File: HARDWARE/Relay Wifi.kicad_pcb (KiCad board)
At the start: 2 copper layers, 43 parts, among them J1 Bornera 01x02, J10 Screw_Terminal_01x03, J11 HC-SR04, J2 Screw_Terminal_01x03, J3 Screw_Terminal_01x03, J4 Screw_Terminal_01x03, J5 Screw_Terminal_01x03, J6 Screw_Terminal_01x03, J7 Screw_Terminal_01x03, J8 Screw_Terminal_01x03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

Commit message: Agrego carpeta hardware con archivos
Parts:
- removed G***: LOGO, LOGO:Logo relé
- removed J10, J5, J6, J7, J8: Screw_Terminal_01x03, TerminalBlock:TerminalBlock_bornier-3_P5.08mm
- removed SW1: SW_SPDT, EESTN5:Pin_Header_3
- added J12: Screw_Terminal_01x04, TerminalBlock_Altech:Altech_AK100_1x04_P5.00mm, F.Cu at (142.0, 39.8)
- added Switch1: SW_SPDT, EESTN5:Pin_Header_3, F.Cu at (157.8, 88.3)
- J1, J11, J9: moved to B.Cu
- J2, J3, J4: value Screw_Terminal_01x03 -> Screw_Terminal_01x04; footprint TerminalBlock:TerminalBlock_bornier-3_P5.08mm -> TerminalBlock_Altech:Altech_AK100_1x04_P5.00mm
- Q1, Q2, Q3, Q4: footprint EESTN5:to92 -> EESTN5:SOT23
- U2, U3, U5, U6: footprint Package_DIP:DIP-4_W7.62mm -> EESTN5:DIP-4_PC817
- U4: footprint Package_TO_SOT_THT:TO-220-3_Vertical -> Package_TO_SOT_SMD:TO-263-3_TabPin2
- moved J4 88.1 mm to (94.9, 39.8), turned to 180 degrees
- moved R4 83.8 mm to (84.0, 125.9)
- moved J3 82.3 mm to (118.4, 39.8), turned to 180 degrees
- moved J11 74.2 mm to (82.7, 129.8)
- moved U3 65.7 mm to (150.4, 70.9), turned to 0 degrees
- moved R1 58.0 mm to (86.5, 125.9), turned to 90 degrees
- moved R3 55.9 mm to (158.0, 77.8)
- moved U2 54.3 mm to (126.7, 70.9), turned to 0 degrees
- moved D2 50.6 mm to (163.0, 70.9), turned to 0 degrees
- moved J9 49.4 mm to (95.6, 129.8), turned to 0 degrees
- moved Q1 46.0 mm to (162.9, 78.8), turned to 90 degrees
- moved R7 44.9 mm to (134.3, 77.8)
- moved R2 44.3 mm to (110.0, 122.5), turned to -90 degrees
- moved R8 43.6 mm to (112.5, 122.5), turned to -90 degrees
- moved U5 42.9 mm to (103.2, 70.9), turned to 0 degrees
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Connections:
- J2 pad 1: com2 -> com3
- J3 pad 1: Net-(J3-Pin_1) -> com5
- J3 pad 3: com3 -> Net-(J3-Pin_3)
- J4 pad 1: com4 -> com7
- K1 pad 11: Net-(J4-Pin_2) -> unconnected-(K1-Pad11)
- K1 pad 6: Net-(J3-Pin_2) -> unconnected-(K1-Pad6)
- K1 pad 8: Net-(J3-Pin_1) -> Net-(J2-Pin_2)
- K1 pad 9: Net-(J4-Pin_3) -> Net-(J2-Pin_3)
- K2 pad 11: Net-(J8-Pin_2) -> unconnected-(K2-Pad11)
- K2 pad 6: Net-(J6-Pin_2) -> unconnected-(K2-Pad6)
- K2 pad 8: Net-(J6-Pin_1) -> Net-(J3-Pin_2)
- K2 pad 9: Net-(J8-Pin_3) -> Net-(J3-Pin_3)
- K3 pad 11: Net-(J2-Pin_2) -> unconnected-(K3-Pad11)
- K3 pad 6: Net-(J10-Pin_2) -> unconnected-(K3-Pad6)
- K3 pad 9: Net-(J2-Pin_3) -> Net-(J12-Pin_3)
- K4 pad 11: Net-(J7-Pin_2) -> unconnected-(K4-Pad11)
- K4 pad 6: Net-(J5-Pin_2) -> unconnected-(K4-Pad6)
- K4 pad 8: Net-(J5-Pin_1) -> Net-(J4-Pin_2)
- K4 pad 9: Net-(J7-Pin_3) -> Net-(J4-Pin_3)
- U1 pad 27: unconnected-(U1-IO16-Pad27) -> relay_4
- U1 pad 28: unconnected-(U1-IO17-Pad28) -> relay_3
- U1 pad 30: unconnected-(U1-IO18-Pad30) -> relay_2
- U1 pad 31: unconnected-(U1-IO19-Pad31) -> relay_1
- U1 pad 4: ECHO -> unconnected-(U1-SVN-Pad4)
- U1 pad 5: relay_2 -> unconnected-(U1-IO34-Pad5)
- U1 pad 6: relay_1 -> unconnected-(U1-IO35-Pad6)
- U1 pad 7: relay_3 -> ECHO
- U1 pad 8: relay_4 -> TRIGGER
- U1 pad 9: TRIGGER -> unconnected-(U1-IO25-Pad9)
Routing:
- net VCC: track 344.5 -> 175.0 mm, vias 5 -> 0
- net GND: track 0.00 -> 144.2 mm, vias 0 -> 6
- net Net-(R10-Pad2): track 9.08 -> 122.9 mm
- net Net-(R6-Pad2): track 38.8 -> 103.7 mm
- net D1: track 47.2 -> 95.0 mm, vias 2 -> 0
- net Net-(R8-Pad2): track 70.8 -> 103.6 mm
- net Net-(J11-Pin_2): track 31.3 -> 2.90 mm, vias 1 -> 0
- net +5V: track 137.6 -> 163.6 mm, vias 1 -> 0
- net ECHO: track 48.1 -> 71.5 mm, vias 1 -> 0
- net Net-(J7-Pin_2): track 16.0 -> 0.00 mm
- net Net-(J5-Pin_2): track 16.0 -> 0.00 mm
- net Net-(J6-Pin_2): track 15.9 -> 0.00 mm
- net Net-(J10-Pin_2): track 15.9 -> 0.00 mm
- net Net-(J8-Pin_2): track 15.9 -> 0.00 mm
- net Net-(D8-A): track 24.5 -> 38.7 mm
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- removed copper zone on B.Cu, net GND

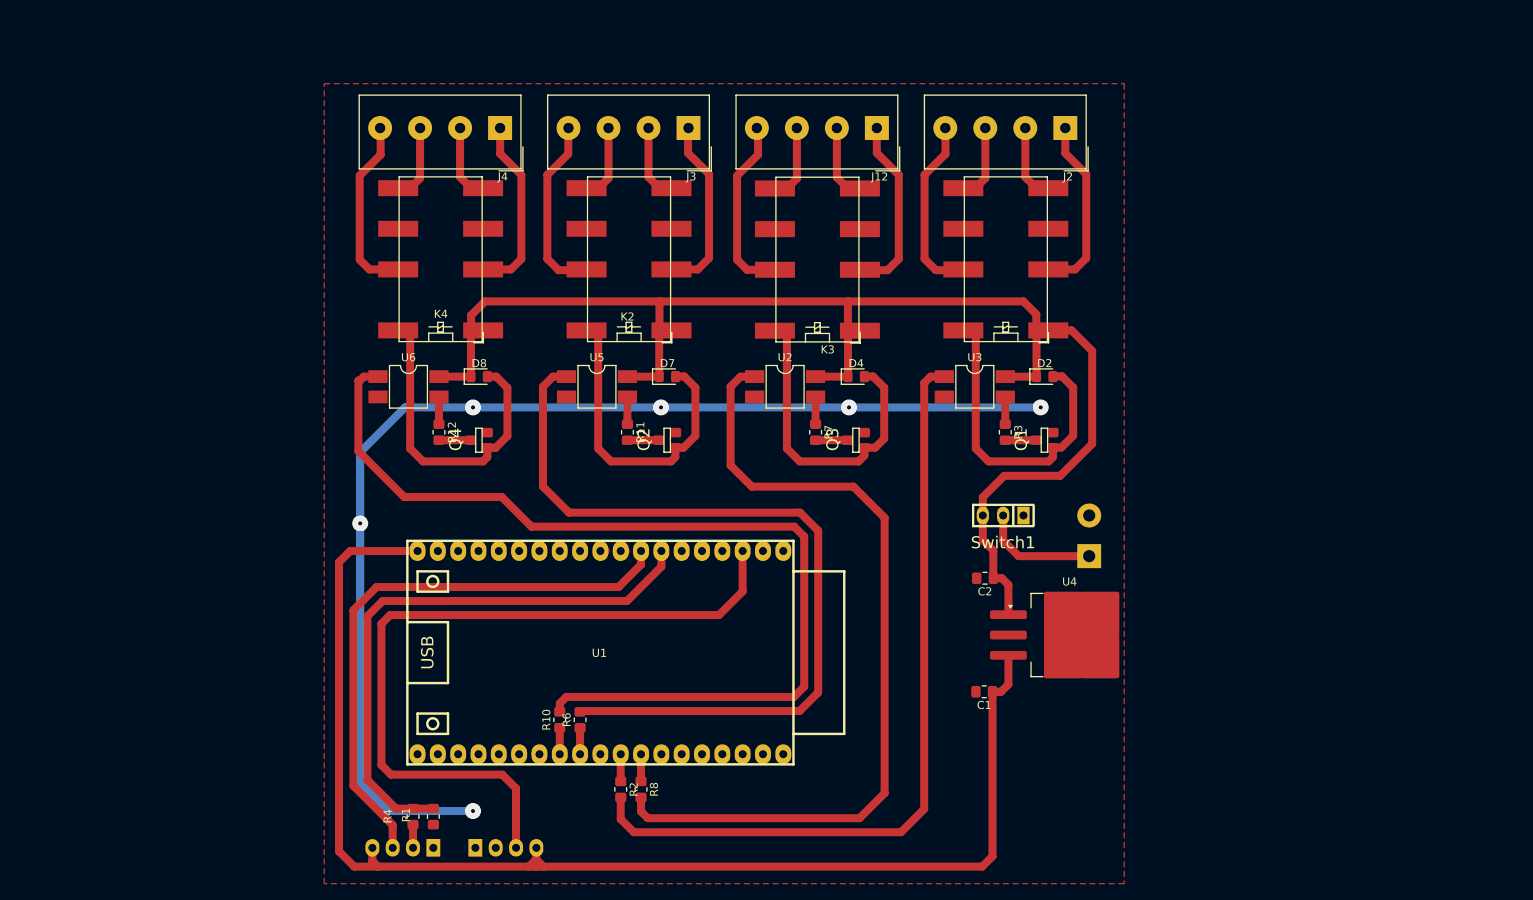
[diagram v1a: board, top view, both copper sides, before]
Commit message: Agrego el nuevo diseño de la placa y el esquematico
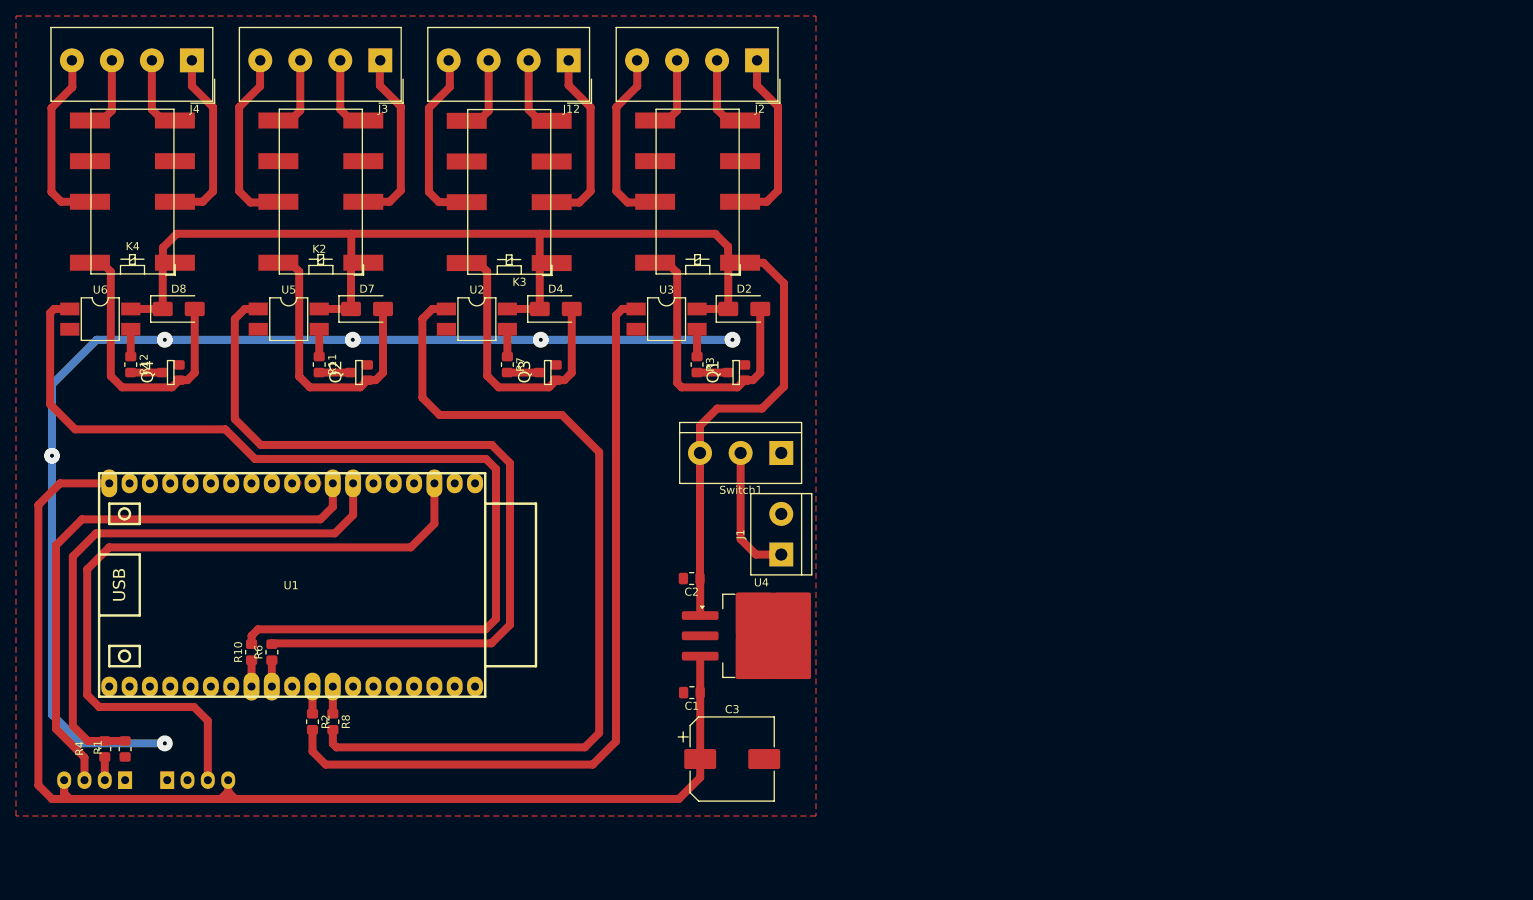
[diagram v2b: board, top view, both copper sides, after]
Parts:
- added C3: C, Capacitor_SMD:CP_Elec_10x10, F.Cu at (123.9, 118.7)
- D2, D4, D7, D8: footprint Diode_SMD:D_0805_2012Metric_Pad1.15x1.40mm_HandSolder -> Diode_SMD:D_SMA
- J1: moved to F.Cu
- Switch1: footprint EESTN5:Pin_Header_3 -> TerminalBlock:TerminalBlock_bornier-3_P5.08mm
- moved U1 39.4 mm to (68.9, 96.9)
- moved J12 39.4 mm to (103.5, 31.4)
- moved K3 39.4 mm to (99.8, 56.7)
- moved J11 39.4 mm to (44.2, 121.3)
- moved J2 39.4 mm to (127.0, 31.4)
- moved J3 39.4 mm to (79.9, 31.4)
- moved J4 39.4 mm to (56.4, 31.4)
- moved K2 39.4 mm to (76.3, 56.7)
- moved K4 39.4 mm to (52.7, 56.7)
- moved Q1 39.4 mm to (124.4, 70.4)
- moved Q2 39.4 mm to (77.2, 70.4)
- moved Q3 39.4 mm to (100.8, 70.4)
- moved Q4 39.4 mm to (53.7, 70.4)
- moved R1 39.4 mm to (48.0, 117.4)
- moved R12 39.4 mm to (48.7, 69.4)
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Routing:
- net +5V: track 163.6 -> 152.3 mm
- net Net-(R8-Pad2): track 103.6 -> 109.4 mm
- net D1: track 95.0 -> 90.4 mm
- net VCC: track 175.0 -> 179.5 mm
- net Net-(D4-A): track 38.8 -> 34.4 mm
- net Net-(D7-A): track 38.7 -> 34.5 mm
- net Net-(D8-A): track 38.7 -> 34.4 mm
- net Net-(D2-A): track 38.7 -> 34.9 mm
- net BAT: track 14.7 -> 16.7 mm
- net ECHO: track 71.5 -> 69.6 mm
- net Net-(R10-Pad2): track 122.9 -> 124.4 mm
- net TRIGGER: track 71.7 -> 70.4 mm
